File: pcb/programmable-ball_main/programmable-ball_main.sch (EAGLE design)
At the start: 34 parts, among them J1 12402012E212A, J3 B4B-ZR-SM4-TFT(LF)(SN), P1 S2B-ZR-SM4A-TF, Q1 DMG2305UX-13, U1 MDBT50Q-1MV2, U2 AP2112K-3.3TRG1, U3 MCP73832T-2ACI/OT, Y1 FC-135_32.7680KA-A0

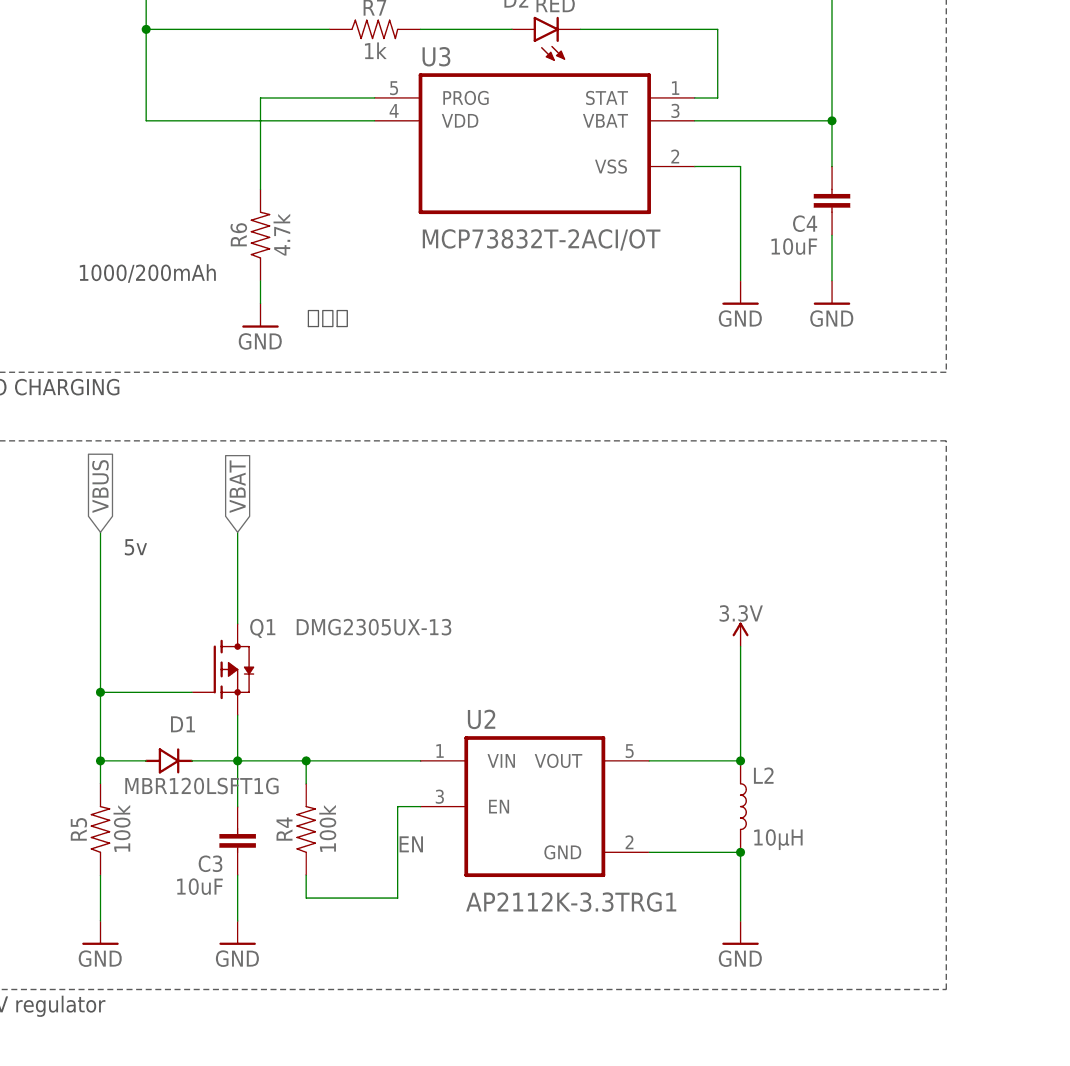
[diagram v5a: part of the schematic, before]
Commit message: シルクの削除
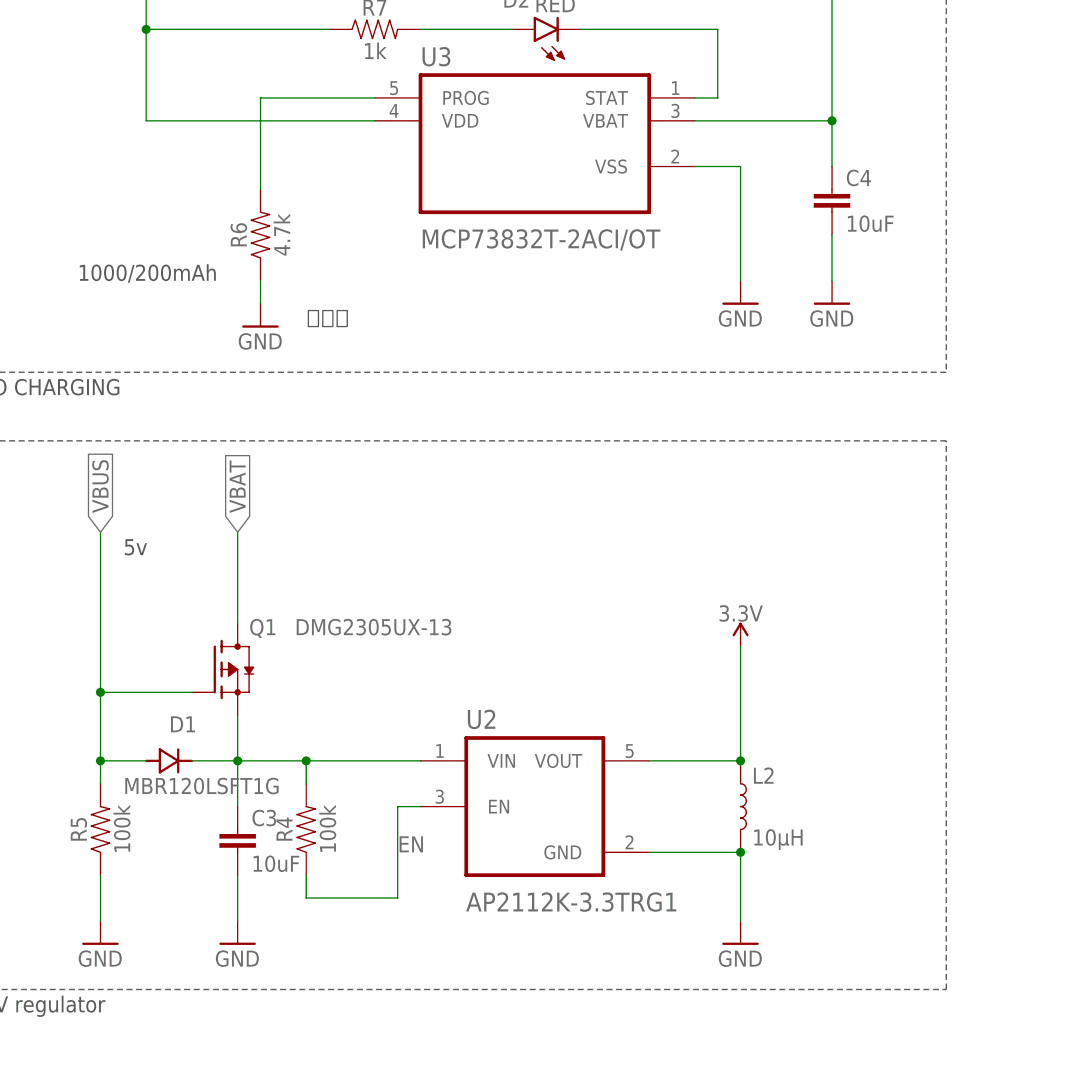
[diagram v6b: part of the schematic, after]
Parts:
- C3, C4, C5, C6: device SparkFun-Capacitors:10UF-0402T-6.3V-20% -> SparkFun-Capacitors:10UF-0603-6.3V-20%
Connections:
- net GND: now also C3.2, C4.2; no longer C3.1, C4.1
- net N$6: now also C3.1; no longer C3.2
- net VBAT: now also C4.1; no longer C4.2
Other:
- moved on the sheet: C3, C4
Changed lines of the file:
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@@
 <part name="GND11" library="supply1" library_urn="urn:adsk.eagle:library:371" deviceset="GND" device=""/>
 <part name="R5" library="SparkFun-Resistors" deviceset="100KOHM" device="-0402T-1/16W-1%" value="100k"/>
-<part name="C3" library="SparkFun-Capacitors" deviceset="10UF" device="-0402T-6.3V-20%" value="10uF"/>
 <part name="SUPPLY4" library="SparkFun-PowerSymbols" deviceset="3.3V" device=""/>
 <part name="GND12" library="supply1" library_urn="urn:adsk.eagle:library:371" deviceset="GND" device=""/>
@@
 <part name="GND15" library="supply1" library_urn="urn:adsk.eagle:library:371" deviceset="GND" device=""/>
 <part name="GND16" library="supply1" library_urn="urn:adsk.eagle:library:371" deviceset="GND" device=""/>
-<part name="C4" library="SparkFun-Capacitors" deviceset="10UF" device="-0402T-6.3V-20%" value="10uF"/>
 <part name="S2" library="CAS_120TA" deviceset="CASA-120TA-PB" device=""/>
 <part name="R6" library="SparkFun-Resistors" deviceset="4.7KOHM" device="-0402T-1/16W-1%" value="4.7k"/>
@@
 <part name="J3" library="B4B-ZR-SM4-TFT_LF__SN_" deviceset="B4B-ZR-SM4-TFT(LF)(SN)" device=""/>
 <part name="GND22" library="supply1" library_urn="urn:adsk.eagle:library:371" deviceset="GND" device=""/>
-<part name="C5" library="SparkFun-Capacitors" deviceset="10UF" device="-0402T-6.3V-20%" value="10uF"/>
-<part name="C6" library="SparkFun-Capacitors" deviceset="10UF" device="-0402T-6.3V-20%" value="10uF"/>
 <part name="C7" library="SparkFun-Capacitors" deviceset="0.1UF" device="-0402T-6.3V-10%-X7R" value="0.1uF"/>
 <part name="C8" library="SparkFun-Capacitors" deviceset="0.1UF" device="-0402T-6.3V-10%-X7R" value="0.1uF"/>
@@
 <part name="R10" library="SparkFun-Resistors" deviceset="100KOHM" device="-0402T-1/16W-1%" value="100k"/>
 <part name="R11" library="SparkFun-Resistors" deviceset="100KOHM" device="-0402T-1/16W-1%" value="100k"/>
+<part name="C3" library="SparkFun-Capacitors" deviceset="10UF" device="-0603-6.3V-20%" value="10uF"/>
+<part name="C4" library="SparkFun-Capacitors" deviceset="10UF" device="-0603-6.3V-20%" value="10uF"/>
+<part name="C5" library="SparkFun-Capacitors" deviceset="10UF" device="-0603-6.3V-20%" value="10uF"/>
+<part name="C6" library="SparkFun-Capacitors" deviceset="10UF" device="-0603-6.3V-20%" value="10uF"/>
 </parts>
 <sheets>
@@
 <attribute name="VALUE" x="39.624" y="58.42" size="1.778" layer="96" font="vector" rot="R90" align="top-center"/>
 </instance>
-<instance part="C3" gate="G$1" x="53.34" y="58.42" smashed="yes" rot="R180">
-<attribute name="NAME" x="51.816" y="55.499" size="1.778" layer="95" font="vector" rot="R180"/>
-<attribute name="VALUE" x="51.816" y="52.959" size="1.778" layer="96" font="vector" rot="R180"/>
-</instance>
 <instance part="SUPPLY4" gate="G$1" x="261.62" y="83.82" smashed="yes">
 <attribute name="VALUE" x="261.62" y="86.614" size="1.778" layer="96" font="vector" align="bottom-center"/>
@@
 <attribute name="VALUE" x="116.84" y="114.3" size="1.778" layer="96"/>
 </instance>
-<instance part="C4" gate="G$1" x="119.38" y="129.54" smashed="yes" rot="R180">
-<attribute name="NAME" x="117.856" y="126.619" size="1.778" layer="95" font="vector" rot="R180"/>
-<attribute name="VALUE" x="117.856" y="124.079" size="1.778" layer="96" font="vector" rot="R180"/>
-</instance>
 <instance part="S2" gate="G$1" x="172.72" y="119.38" smashed="yes" rot="R270">
 <attribute name="NAME" x="175.768" y="118.11" size="1.778" layer="95" font="vector" rot="R270" align="bottom-center"/>
@@
 <attribute name="VALUE" x="33.02" y="193.04" size="1.778" layer="96"/>
 </instance>
+<instance part="C7" gate="G$1" x="81.28" y="208.28" smashed="yes">
+<attribute name="NAME" x="82.804" y="211.201" size="1.778" layer="95" font="vector"/>
+<attribute name="VALUE" x="82.804" y="206.121" size="1.778" layer="96" font="vector"/>
+</instance>
+<instance part="C8" gate="G$1" x="66.04" y="208.28" smashed="yes">
+<attribute name="NAME" x="67.564" y="211.201" size="1.778" layer="95" font="vector"/>
+<attribute name="VALUE" x="67.564" y="206.121" size="1.778" layer="96" font="vector"/>
+</instance>
+<instance part="R8" gate="G$1" x="340.36" y="182.88" smashed="yes">
+<attribute name="NAME" x="337.82" y="184.404" size="1.778" layer="95" font="vector" align="bottom-center"/>
+<attribute name="VALUE" x="342.9" y="186.436" size="1.778" layer="96" font="vector" align="top-center"/>
+</instance>
+<instance part="R9" gate="G$1" x="340.36" y="180.34" smashed="yes">
+<attribute name="NAME" x="337.82" y="176.784" size="1.778" layer="95" font="vector" align="bottom-center"/>
+<attribute name="VALUE" x="342.9" y="178.816" size="1.778" layer="96" font="vector" align="top-center"/>
+</instance>
+<instance part="R10" gate="G$1" x="193.04" y="180.34" smashed="yes" rot="R90">
+<attribute name="NAME" x="191.516" y="180.34" size="1.778" layer="95" font="vector" rot="R90" align="bottom-center"/>
+<attribute name="VALUE" x="194.564" y="180.34" size="1.778" layer="96" font="vector" rot="R90" align="top-center"/>
+</instance>
+<instance part="R11" gate="G$1" x="193.04" y="165.1" smashed="yes" rot="R90">
+<attribute name="NAME" x="191.516" y="165.1" size="1.778" layer="95" font="vector" rot="R90" align="bottom-center"/>
+<attribute name="VALUE" x="194.564" y="165.1" size="1.778" layer="96" font="vector" rot="R90" align="top-center"/>
+</instance>
+<instance part="C3" gate="G$1" x="53.34" y="55.88" smashed="yes">
+<attribute name="NAME" x="54.864" y="58.801" size="1.778" layer="95" font="vector"/>
+<attribute name="VALUE" x="54.864" y="53.721" size="1.778" layer="96" font="vector"/>
+</instance>
+<instance part="C4" gate="G$1" x="119.38" y="127" smashed="yes">
+<attribute name="NAME" x="120.904" y="129.921" size="1.778" layer="95" font="vector"/>
+<attribute name="VALUE" x="120.904" y="124.841" size="1.778" layer="96" font="vector"/>
+</instance>
 <instance part="C5" gate="G$1" x="55.88" y="208.28" smashed="yes">
 <attribute name="NAME" x="57.404" y="211.201" size="1.778" layer="95" font="vector"/>
@@
 <attribute name="NAME" x="37.084" y="211.201" size="1.778" layer="95" font="vector"/>
 <attribute name="VALUE" x="37.084" y="206.121" size="1.778" layer="96" font="vector"/>
-</instance>
-<instance part="C7" gate="G$1" x="81.28" y="208.28" smashed="yes">
-<attribute name="NAME" x="82.804" y="211.201" size="1.778" layer="95" font="vector"/>
-<attribute name="VALUE" x="82.804" y="206.121" size="1.778" layer="96" font="vector"/>
-</instance>
-<instance part="C8" gate="G$1" x="66.04" y="208.28" smashed="yes">
-<attribute name="NAME" x="67.564" y="211.201" size="1.778" layer="95" font="vector"/>
-<attribute name="VALUE" x="67.564" y="206.121" size="1.778" layer="96" font="vector"/>
-</instance>
-<instance part="R8" gate="G$1" x="340.36" y="182.88" smashed="yes">
-<attribute name="NAME" x="337.82" y="184.404" size="1.778" layer="95" font="vector" align="bottom-center"/>
-<attribute name="VALUE" x="342.9" y="186.436" size="1.778" layer="96" font="vector" align="top-center"/>
-</instance>
-<instance part="R9" gate="G$1" x="340.36" y="180.34" smashed="yes">
-<attribute name="NAME" x="337.82" y="176.784" size="1.778" layer="95" font="vector" align="bottom-center"/>
-<attribute name="VALUE" x="342.9" y="178.816" size="1.778" layer="96" font="vector" align="top-center"/>
-</instance>
-<instance part="R10" gate="G$1" x="193.04" y="180.34" smashed="yes" rot="R90">
-<attribute name="NAME" x="191.516" y="180.34" size="1.778" layer="95" font="vector" rot="R90" align="bottom-center"/>
-<attribute name="VALUE" x="194.564" y="180.34" size="1.778" layer="96" font="vector" rot="R90" align="top-center"/>
-</instance>
-<instance part="R11" gate="G$1" x="193.04" y="165.1" smashed="yes" rot="R90">
-<attribute name="NAME" x="191.516" y="165.1" size="1.778" layer="95" font="vector" rot="R90" align="bottom-center"/>
-<attribute name="VALUE" x="194.564" y="165.1" size="1.778" layer="96" font="vector" rot="R90" align="top-center"/>
 </instance>
 </instances>
@@
 </segment>
 <segment>
-<pinref part="C3" gate="G$1" pin="1"/>
 <pinref part="GND10" gate="1" pin="GND"/>
 <wire x1="53.34" y1="53.34" x2="53.34" y2="48.26" width="0.1524" layer="91"/>
+<pinref part="C3" gate="G$1" pin="2"/>
 </segment>
 <segment>
@@
 </segment>
 <segment>
-<pinref part="C4" gate="G$1" pin="1"/>
 <pinref part="GND16" gate="1" pin="GND"/>
 <wire x1="119.38" y1="124.46" x2="119.38" y2="119.38" width="0.1524" layer="91"/>
+<pinref part="C4" gate="G$1" pin="2"/>
 </segment>
 <segment>
@@
 <wire x1="104.14" y1="137.16" x2="119.38" y2="137.16" width="0.1524" layer="91"/>
 <wire x1="119.38" y1="137.16" x2="119.38" y2="157.48" width="0.1524" layer="91"/>
-<pinref part="C4" gate="G$1" pin="2"/>
 <wire x1="119.38" y1="137.16" x2="119.38" y2="132.08" width="0.1524" layer="91"/>
 <junction x="119.38" y="137.16"/>
+<pinref part="C4" gate="G$1" pin="1"/>
 </segment>
 <segment>
@@
 <pinref part="Q1" gate="G$1" pin="S"/>
 <wire x1="53.34" y1="71.12" x2="53.34" y2="66.04" width="0.1524" layer="91"/>
-<pinref part="C3" gate="G$1" pin="2"/>
 <wire x1="53.34" y1="66.04" x2="53.34" y2="60.96" width="0.1524" layer="91"/>
 <junction x="53.34" y="66.04"/>
 <pinref part="D1" gate="G$1" pin="C"/>
 <wire x1="48.26" y1="66.04" x2="53.34" y2="66.04" width="0.1524" layer="91"/>
-</segment>
-</net>
+<pinref part="C3" gate="G$1" pin="1"/>
+</segment>
+</net>
